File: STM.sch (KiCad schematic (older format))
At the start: 17 parts, among them J3 Micro_SD_Card_Det, J4 TagConnect_TC2030_SWD, Q9 AO3401A, SW8 POWER, U8 STM32L151C8Tx

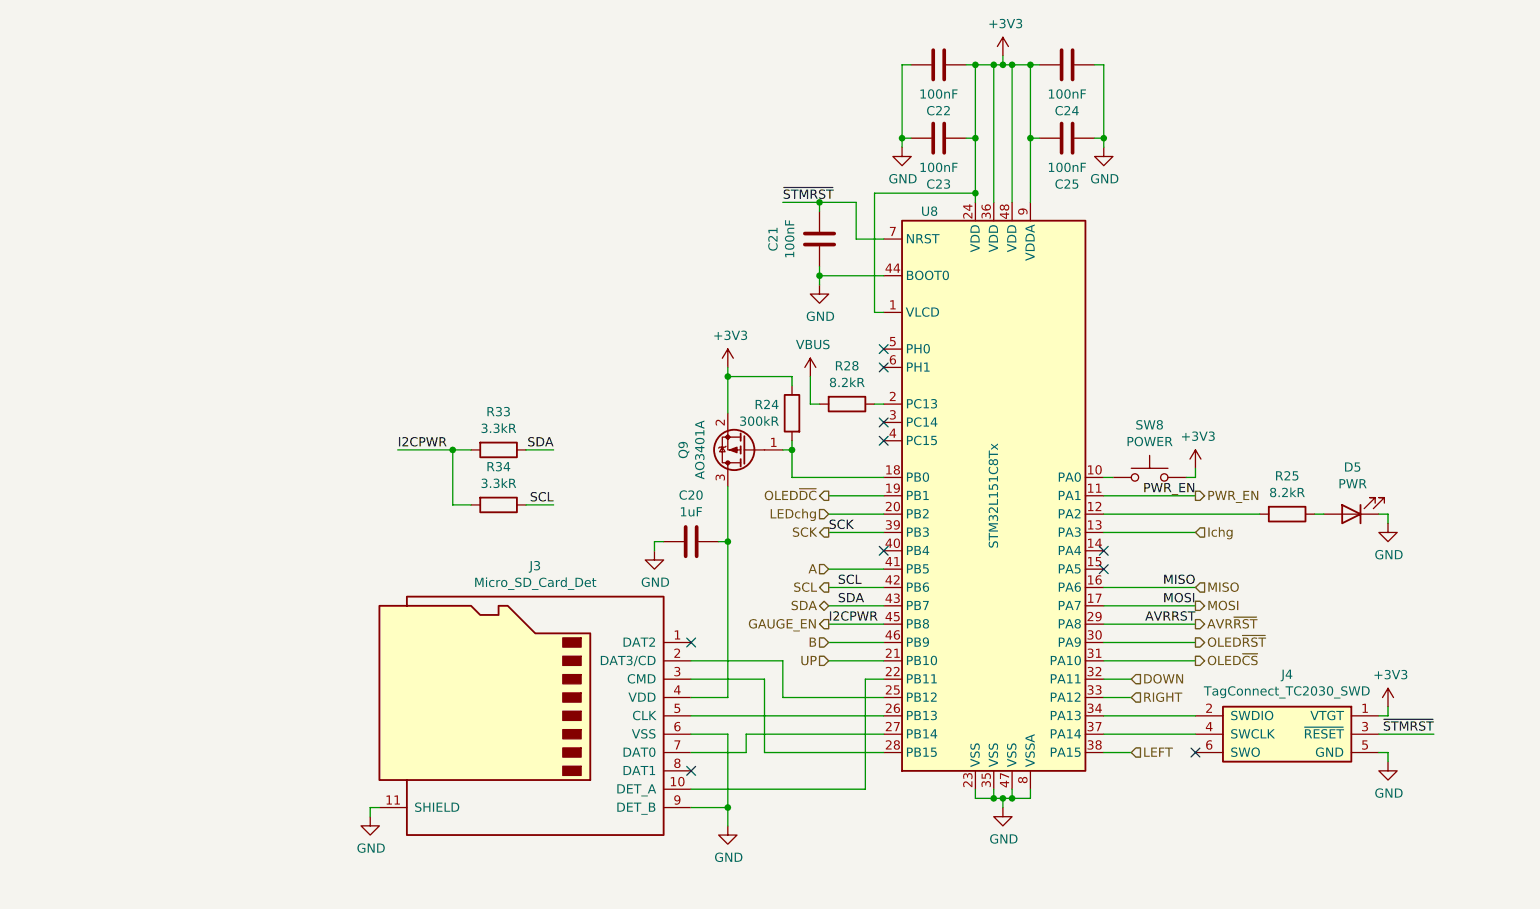
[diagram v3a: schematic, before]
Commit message: Route SD interface
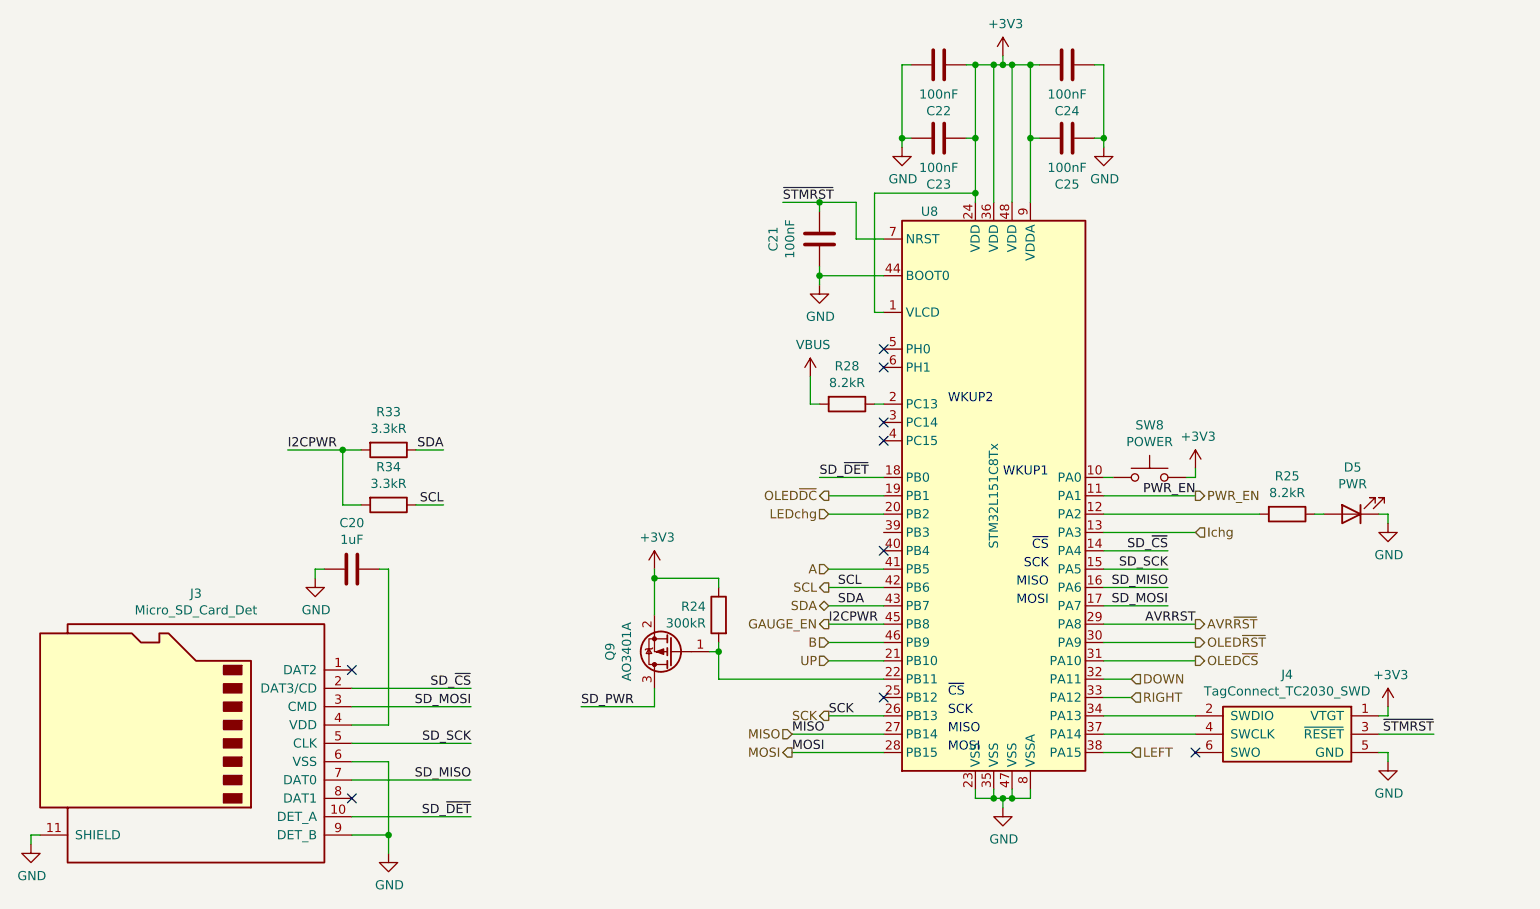
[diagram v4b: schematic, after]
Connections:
- net MISO: now also U8.27 (PB14); no longer U8.16 (PA6)
- net MOSI: now also U8.28 (PB15); no longer U8.17 (PA7)
- net SCK: now also U8.26 (PB13); no longer U8.39 (PB3)
- net SD_~CS: now reaches U8.14 (PA4)
- net SD_~CS: now also J3.2 (DAT3/CD)
- net SD_SCK: now reaches U8.15 (PA5)
- net SD_SCK: now also J3.5 (CLK)
- net at Q9.1 (G), R24.2: now also U8.22 (PB11); no longer U8.18 (PB0)
- net SD_~DET: now reaches J3.10 (DET_A)
- net SD_~DET: now also U8.18 (PB0); no longer U8.22 (PB11)
- net at U8.25 (PB12): no longer J3.2 (DAT3/CD)
- net SD_MISO: now reaches J3.7 (DAT0)
- net SD_MISO: now also U8.16 (PA6); no longer U8.27 (PB14)
- net SD_MOSI: now reaches J3.3 (CMD)
- net SD_MOSI: now also U8.17 (PA7); no longer U8.28 (PB15)
- net at C20.1, J3.4 (VDD): no longer Q9.3 (D)
- new net SD_PWR: Q9.3 (D)
- no-connect marks 10 -> 9
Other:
- note added: "MISO"
- note added: "MOSI"
- note added: "SCK"
- note added: "WKUP1"
- note added: "WKUP2"
- note added: "~CS"
- moved on the sheet: C20, J3, Q9, R24, R33, R34

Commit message: Hookup VFD
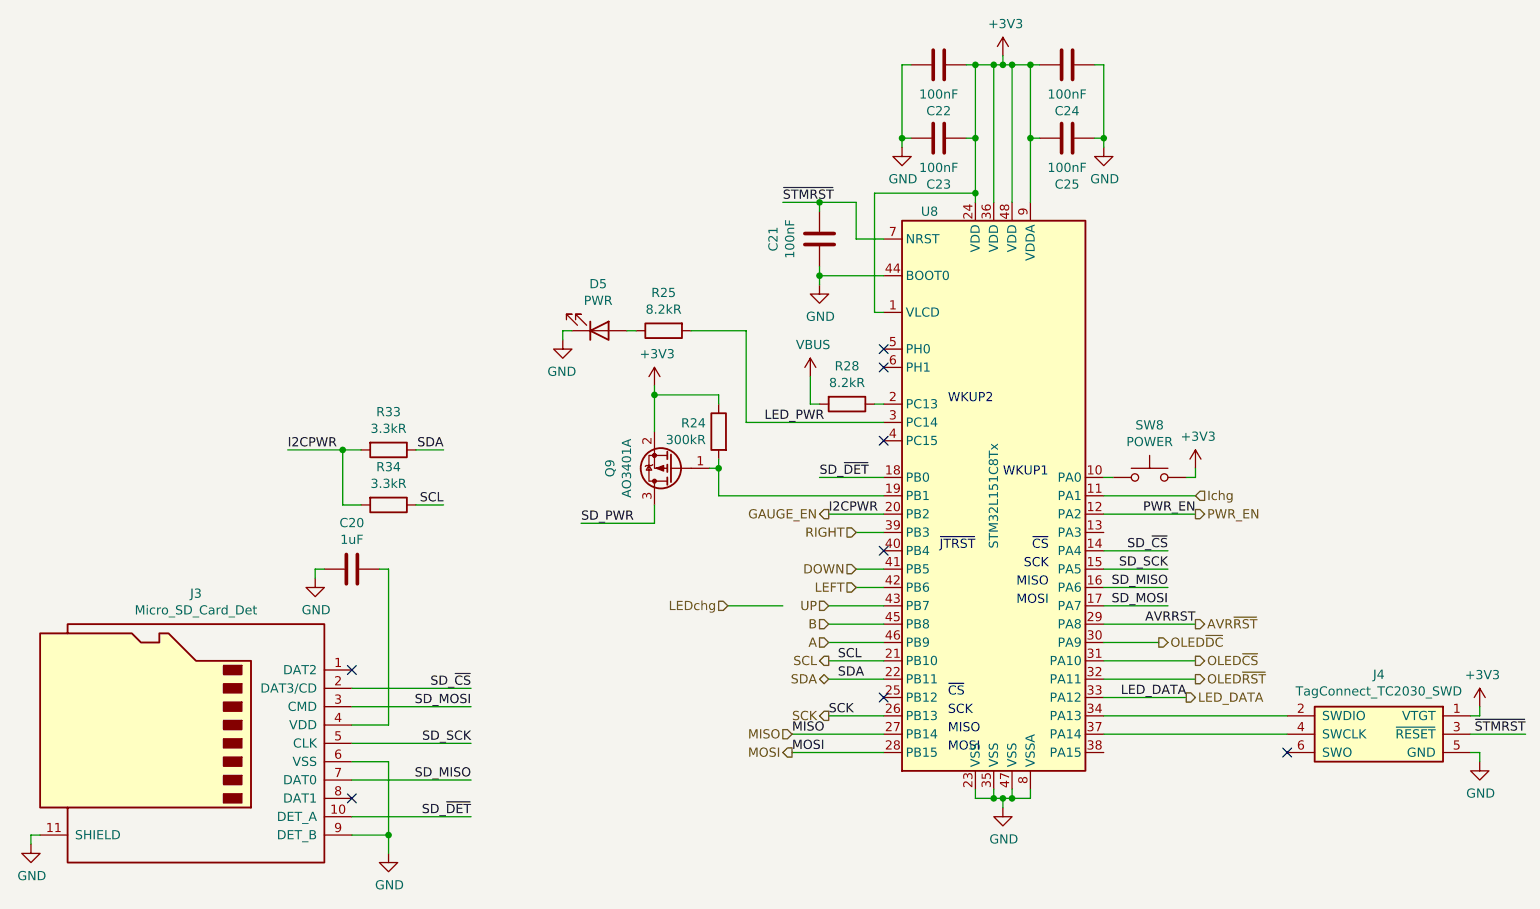
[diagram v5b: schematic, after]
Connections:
- net A: now also U8.46 (PB9); no longer U8.41 (PB5)
- net B: now also U8.45 (PB8); no longer U8.46 (PB9)
- net DOWN: now also U8.41 (PB5); no longer U8.32 (PA11)
- net GAUGE_EN: now also U8.20 (PB2); no longer U8.45 (PB8)
- net Ichg: now also U8.11 (PA1); no longer U8.13 (PA3)
- net LEDchg: no longer U8.20 (PB2)
- net LEFT: now also U8.42 (PB6); no longer U8.38 (PA15)
- net OLED~DC: now also U8.30 (PA9); no longer U8.19 (PB1)
- net OLED~RST: now also U8.32 (PA11); no longer U8.30 (PA9)
- net PWR_EN: now also U8.12 (PA2); no longer U8.11 (PA1)
- net RIGHT: now also U8.39 (PB3); no longer U8.33 (PA12)
- net SCL: now also U8.21 (PB10); no longer U8.42 (PB6)
- net SDA: now also U8.22 (PB11); no longer U8.43 (PB7)
- net UP: now also U8.43 (PB7); no longer U8.21 (PB10)
- net LED_PWR: now reaches R25.2
- net LED_PWR: now also U8.3 (PC14); no longer U8.12 (PA2)
- net at Q9.1 (G), R24.2: now also U8.19 (PB1); no longer U8.22 (PB11)
- new net LED_DATA: U8.33 (PA12)
- no-connect marks 9 -> 8
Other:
- note added: "~JTRST"
- moved on the sheet: D5, J4, Q9, R24, R25

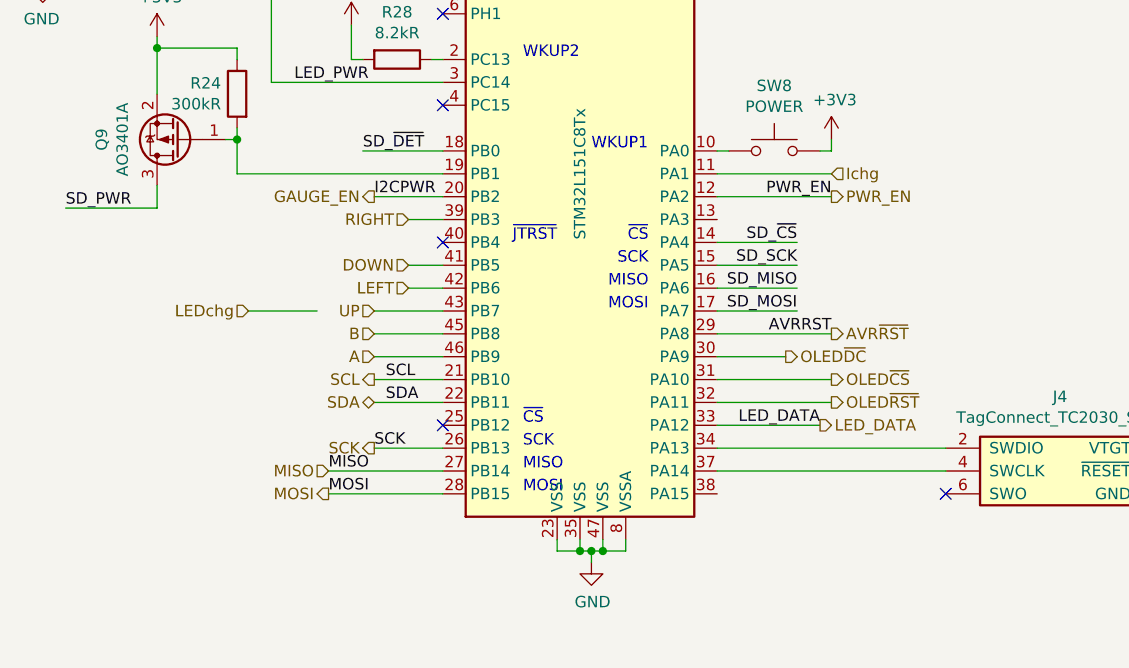
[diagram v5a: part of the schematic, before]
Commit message: Connect buttons
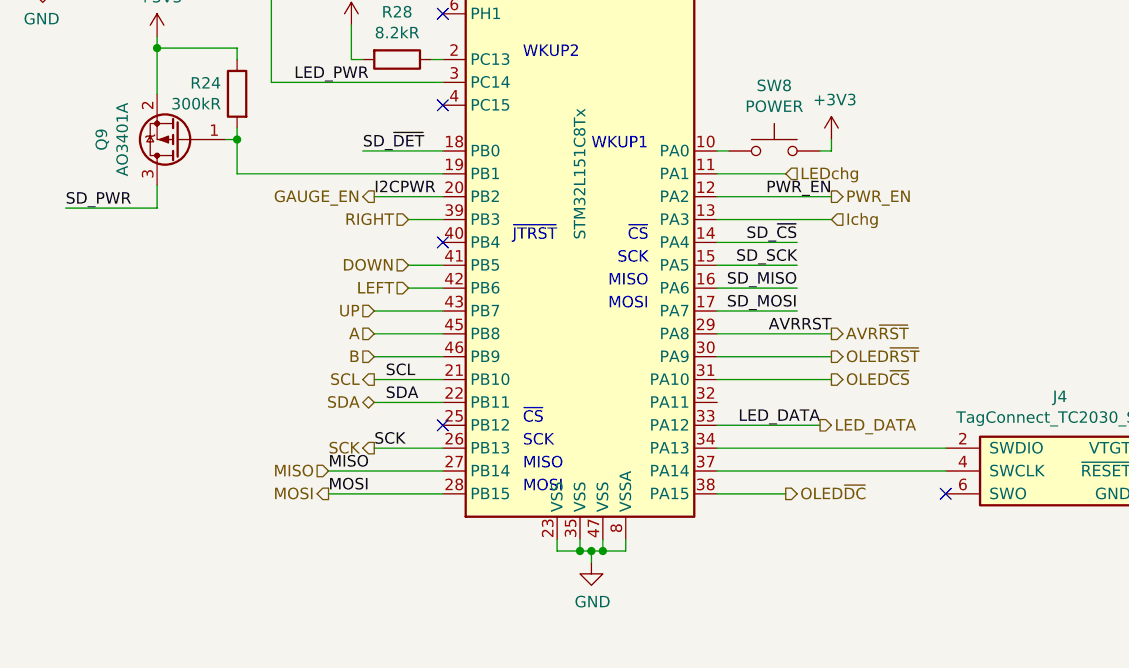
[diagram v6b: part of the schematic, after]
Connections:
- net A: now also U8.45 (PB8); no longer U8.46 (PB9)
- net B: now also U8.46 (PB9); no longer U8.45 (PB8)
- net Ichg: now also U8.13 (PA3); no longer U8.11 (PA1)
- net LEDchg: now also U8.11 (PA1)
- net OLED~DC: now also U8.38 (PA15); no longer U8.30 (PA9)
- net OLED~RST: now also U8.30 (PA9); no longer U8.32 (PA11)
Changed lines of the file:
@@
 	5150 5100 5450 5100
 Wire Wire Line
-	6650 4900 7150 4900
-Text HLabel 7150 4900 2    50   Output ~ 0
+	6650 4700 7150 4700
+Text HLabel 7150 4700 2    50   Output ~ 0
 OLED~RST
 Wire Wire Line
@@
 OLED~CS
 Wire Wire Line
-	6650 4700 6950 4700
-Text HLabel 6950 4700 2    50   Output ~ 0
+	6650 5300 6950 5300
+Text HLabel 6950 5300 2    50   Output ~ 0
 OLED~DC
 $Comp
@@
 	5050 3400 5100 3400
 Wire Wire Line
-	6650 3900 7150 3900
-Text HLabel 7150 3900 2    50   Input ~ 0
+	6650 4100 7150 4100
+Text HLabel 7150 4100 2    50   Input ~ 0
 Ichg
 Wire Wire Line
-	4900 4500 4600 4500
-Text HLabel 4600 4500 0    50   Input ~ 0
+	6650 3900 6950 3900
+Text HLabel 6950 3900 2    50   Input ~ 0
 LEDchg
 Wire Wire Line
@@
 SCL
 Wire Wire Line
+	5450 4600 5150 4600
+Text HLabel 5150 4600 0    50   Input ~ 0
+A
+Wire Wire Line
 	5450 4700 5150 4700
 Text HLabel 5150 4700 0    50   Input ~ 0
-A
-Wire Wire Line
-	5450 4600 5150 4600
-Text HLabel 5150 4600 0    50   Input ~ 0
 B
 Wire Wire Line
